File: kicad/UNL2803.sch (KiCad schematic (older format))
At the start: 19 parts, among them P15 CONN_01X08, P16 CONN_01X08, U4 ULN2803

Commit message: cambios menores
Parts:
- D10, D11, D12, D13, D6, D7, D8, D9: symbol LED -> LED-RESCUE-np08
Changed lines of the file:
@@
 EESchema Schematic File Version 2
+LIBS:np08-rescue
 LIBS:power
 LIBS:device
@@
 	7300 4500 6900 4500
 $Comp
-L LED D6
+L LED-RESCUE-np08 D6
 U 1 1 57A4DC0A
 P 7900 3800
+AR Path="/57A4DC0A" Ref="D6"  Part="1"
+AR Path="/57A4D8D4/57A4DC0A" Ref="D6"  Part="1"
 F 0 "D6" H 7900 3900 50  0000 C CNN
 F 1 "LED" H 7900 3700 50  0000 C CNN
@@
 $EndComp
 $Comp
-L LED D7
+L LED-RESCUE-np08 D7
 U 1 1 57A4DC4B
 P 8200 3900
+AR Path="/57A4DC4B" Ref="D7"  Part="1"
+AR Path="/57A4D8D4/57A4DC4B" Ref="D7"  Part="1"
 F 0 "D7" H 8200 4000 50  0000 C CNN
 F 1 "LED" H 8200 3800 50  0000 C CNN
@@
 $EndComp
 $Comp
-L LED D8
+L LED-RESCUE-np08 D8
 U 1 1 57A4DC8A
 P 8500 4000
+AR Path="/57A4DC8A" Ref="D8"  Part="1"
+AR Path="/57A4D8D4/57A4DC8A" Ref="D8"  Part="1"
 F 0 "D8" H 8500 4100 50  0000 C CNN
 F 1 "LED" H 8500 3900 50  0000 C CNN
@@
 $EndComp
 $Comp
-L LED D9
+L LED-RESCUE-np08 D9
 U 1 1 57A4DCFC
 P 8800 4100
+AR Path="/57A4DCFC" Ref="D9"  Part="1"
+AR Path="/57A4D8D4/57A4DCFC" Ref="D9"  Part="1"
 F 0 "D9" H 8800 4200 50  0000 C CNN
 F 1 "LED" H 8800 4000 50  0000 C CNN
@@
 $EndComp
 $Comp
-L LED D10
+L LED-RESCUE-np08 D10
 U 1 1 57A4DE04
 P 9100 4200
+AR Path="/57A4DE04" Ref="D10"  Part="1"
+AR Path="/57A4D8D4/57A4DE04" Ref="D10"  Part="1"
 F 0 "D10" H 9100 4300 50  0000 C CNN
 F 1 "LED" H 9100 4100 50  0000 C CNN
@@
 $EndComp
 $Comp
-L LED D11
+L LED-RESCUE-np08 D11
 U 1 1 57A4DE4E
 P 9400 4300
+AR Path="/57A4DE4E" Ref="D11"  Part="1"
+AR Path="/57A4D8D4/57A4DE4E" Ref="D11"  Part="1"
 F 0 "D11" H 9400 4400 50  0000 C CNN
 F 1 "LED" H 9400 4200 50  0000 C CNN
@@
 $EndComp
 $Comp
-L LED D12
+L LED-RESCUE-np08 D12
 U 1 1 57A4DEA5
 P 9700 4400
+AR Path="/57A4DEA5" Ref="D12"  Part="1"
+AR Path="/57A4D8D4/57A4DEA5" Ref="D12"  Part="1"
 F 0 "D12" H 9700 4500 50  0000 C CNN
 F 1 "LED" H 9700 4300 50  0000 C CNN
@@
 	9500 4400 7400 4400
 $Comp
-L LED D13
+L LED-RESCUE-np08 D13
 U 1 1 57A4E19D
 P 10000 4500
+AR Path="/57A4E19D" Ref="D13"  Part="1"
+AR Path="/57A4D8D4/57A4E19D" Ref="D13"  Part="1"
 F 0 "D13" H 10000 4600 50  0000 C CNN
 F 1 "LED" H 10000 4400 50  0000 C CNN

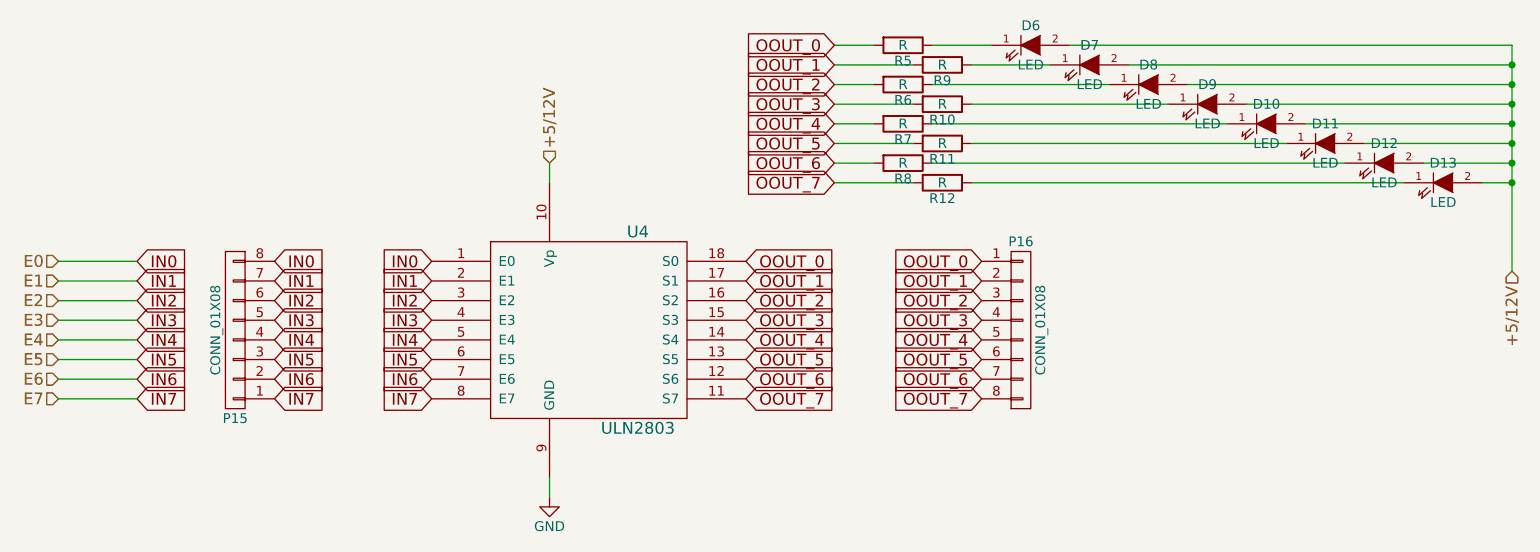
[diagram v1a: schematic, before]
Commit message: cambios en la placa np08
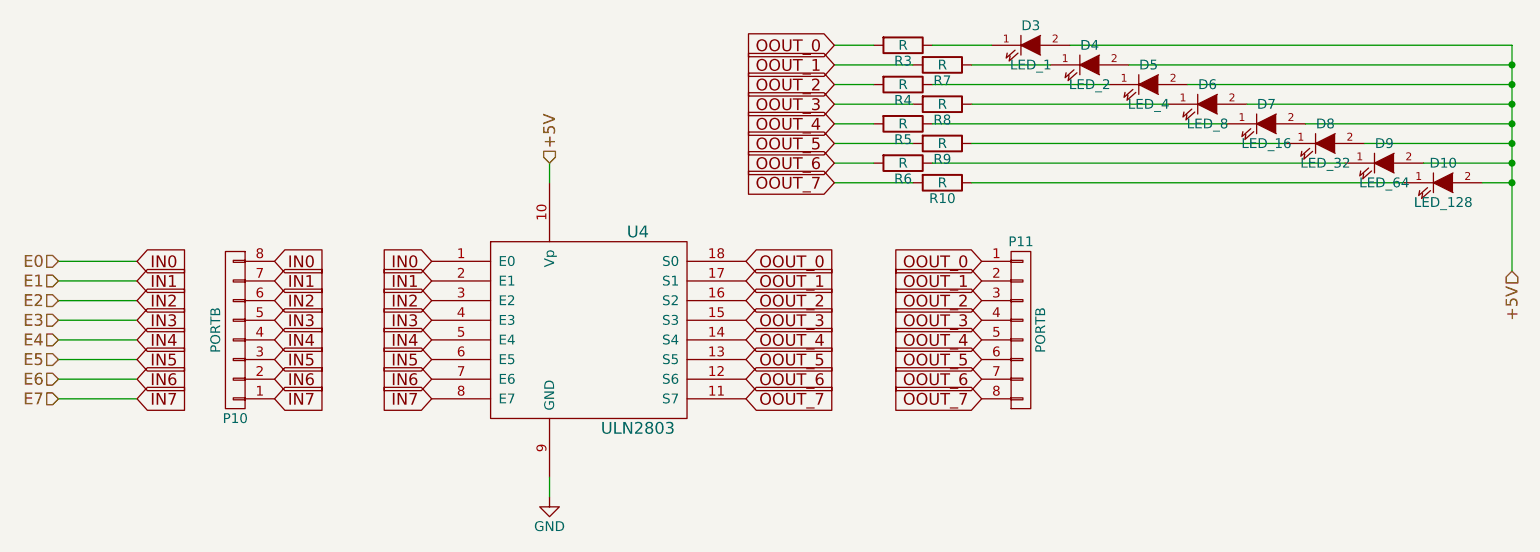
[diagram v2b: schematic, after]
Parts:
- D10: renamed from D13; value LED -> LED_128; footprint LEDs:LED-5MM -> LEDs:LED_D5.0mm
- D3: renamed from D6; value LED -> LED_1; footprint LEDs:LED-5MM -> LEDs:LED_D5.0mm
- D4: renamed from D7; value LED -> LED_2; footprint LEDs:LED-5MM -> LEDs:LED_D5.0mm
- D5: renamed from D8; value LED -> LED_4; footprint LEDs:LED-5MM -> LEDs:LED_D5.0mm
- D6: renamed from D9; value LED -> LED_8; footprint LEDs:LED-5MM -> LEDs:LED_D5.0mm
- D7: renamed from D10; value LED -> LED_16; footprint LEDs:LED-5MM -> LEDs:LED_D5.0mm
- D8: renamed from D11; value LED -> LED_32; footprint LEDs:LED-5MM -> LEDs:LED_D5.0mm
- D9: renamed from D12; value LED -> LED_64; footprint LEDs:LED-5MM -> LEDs:LED_D5.0mm
- P10: renamed from P15; value CONN_01X08 -> PORTB; footprint Pin_Headers:Pin_Header_Straight_1x08 -> Pin_Headers:Pin_Header_Straight_1x08_Pitch2.54mm
- P11: renamed from P16; value CONN_01X08 -> PORTB; footprint Pin_Headers:Pin_Header_Straight_1x08 -> Pin_Headers:Pin_Header_Straight_1x08_Pitch2.54mm
- R10: renamed from R12; footprint Resistors_ThroughHole:Resistor_Horizontal_RM7mm -> Resistors_THT:R_Axial_DIN0411_L9.9mm_D3.6mm_P12.70mm_Horizontal
- R3: renamed from R5; footprint Resistors_ThroughHole:Resistor_Horizontal_RM7mm -> Resistors_THT:R_Axial_DIN0411_L9.9mm_D3.6mm_P12.70mm_Horizontal
- R4: renamed from R6; footprint Resistors_ThroughHole:Resistor_Horizontal_RM7mm -> Resistors_THT:R_Axial_DIN0411_L9.9mm_D3.6mm_P12.70mm_Horizontal
- R5: renamed from R7; footprint Resistors_ThroughHole:Resistor_Horizontal_RM7mm -> Resistors_THT:R_Axial_DIN0411_L9.9mm_D3.6mm_P12.70mm_Horizontal
- R6: renamed from R8; footprint Resistors_ThroughHole:Resistor_Horizontal_RM7mm -> Resistors_THT:R_Axial_DIN0411_L9.9mm_D3.6mm_P12.70mm_Horizontal
- R7: renamed from R9; footprint Resistors_ThroughHole:Resistor_Horizontal_RM7mm -> Resistors_THT:R_Axial_DIN0411_L9.9mm_D3.6mm_P12.70mm_Horizontal
- R8: renamed from R10; footprint Resistors_ThroughHole:Resistor_Horizontal_RM7mm -> Resistors_THT:R_Axial_DIN0411_L9.9mm_D3.6mm_P12.70mm_Horizontal
- R9: renamed from R11; footprint Resistors_ThroughHole:Resistor_Horizontal_RM7mm -> Resistors_THT:R_Axial_DIN0411_L9.9mm_D3.6mm_P12.70mm_Horizontal
- U4: footprint Housings_DIP:DIP-18_W7.62mm -> Housings_DIP:DIP-18_W7.62mm_LongPads
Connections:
- net +5/12V renamed +5V
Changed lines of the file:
@@
 F 0 "U4" H 5900 5750 60  0000 C CNN
 F 1 "ULN2803" H 5900 4750 60  0000 C CNN
-F 2 "Housings_DIP:DIP-18_W7.62mm" H 5650 5250 60  0001 C CNN
+F 2 "Housings_DIP:DIP-18_W7.62mm_LongPads" H 5650 5250 60  0001 C CNN
 F 3 "" H 5650 5250 60  0000 C CNN
 	1    5650 5250
@@
 $EndComp
 $Comp
-L GND #PWR022
+L GND #PWR033
 U 1 1 57A4D9B4
 P 5450 6100
-F 0 "#PWR022" H 5450 5850 50  0001 C CNN
+F 0 "#PWR033" H 5450 5850 50  0001 C CNN
 F 1 "GND" H 5450 5950 50  0000 C CNN
 F 2 "" H 5450 6100 50  0000 C CNN
@@
 	5450 6100 5450 6000
 $Comp
-L R R5
+L R R3
 U 1 1 57A4D9CE
 P 7250 3800
-F 0 "R5" V 7330 3800 50  0000 C CNN
+F 0 "R3" V 7330 3800 50  0000 C CNN
 F 1 "R" V 7250 3800 50  0000 C CNN
-F 2 "Resistors_ThroughHole:Resistor_Horizontal_RM7mm" V 7180 3800 50  0001 C CNN
+F 2 "Resistors_THT:R_Axial_DIN0411_L9.9mm_D3.6mm_P12.70mm_Horizontal" V 7180 3800 50  0001 C CNN
 F 3 "" H 7250 3800 50  0000 C CNN
 	1    7250 3800
@@
 $EndComp
 $Comp
-L R R9
+L R R7
 U 1 1 57A4DA37
 P 7450 3900
-F 0 "R9" V 7530 3900 50  0000 C CNN
+F 0 "R7" V 7530 3900 50  0000 C CNN
 F 1 "R" V 7450 3900 50  0000 C CNN
-F 2 "Resistors_ThroughHole:Resistor_Horizontal_RM7mm" V 7380 3900 50  0001 C CNN
+F 2 "Resistors_THT:R_Axial_DIN0411_L9.9mm_D3.6mm_P12.70mm_Horizontal" V 7380 3900 50  0001 C CNN
 F 3 "" H 7450 3900 50  0000 C CNN
 	1    7450 3900
@@
 $EndComp
 $Comp
-L R R6
+L R R4
 U 1 1 57A4DA6C
 P 7250 4000
-F 0 "R6" V 7330 4000 50  0000 C CNN
+F 0 "R4" V 7330 4000 50  0000 C CNN
 F 1 "R" V 7250 4000 50  0000 C CNN
-F 2 "Resistors_ThroughHole:Resistor_Horizontal_RM7mm" V 7180 4000 50  0001 C CNN
+F 2 "Resistors_THT:R_Axial_DIN0411_L9.9mm_D3.6mm_P12.70mm_Horizontal" V 7180 4000 50  0001 C CNN
 F 3 "" H 7250 4000 50  0000 C CNN
 	1    7250 4000
@@
 $EndComp
 $Comp
-L R R10
+L R R8
 U 1 1 57A4DA94
 P 7450 4100
-F 0 "R10" V 7530 4100 50  0000 C CNN
+F 0 "R8" V 7530 4100 50  0000 C CNN
 F 1 "R" V 7450 4100 50  0000 C CNN
-F 2 "Resistors_ThroughHole:Resistor_Horizontal_RM7mm" V 7380 4100 50  0001 C CNN
+F 2 "Resistors_THT:R_Axial_DIN0411_L9.9mm_D3.6mm_P12.70mm_Horizontal" V 7380 4100 50  0001 C CNN
 F 3 "" H 7450 4100 50  0000 C CNN
 	1    7450 4100
@@
 $EndComp
 $Comp
-L R R7
+L R R5
 U 1 1 57A4DABB
 P 7250 4200
-F 0 "R7" V 7330 4200 50  0000 C CNN
+F 0 "R5" V 7330 4200 50  0000 C CNN
 F 1 "R" V 7250 4200 50  0000 C CNN
-F 2 "Resistors_ThroughHole:Resistor_Horizontal_RM7mm" V 7180 4200 50  0001 C CNN
+F 2 "Resistors_THT:R_Axial_DIN0411_L9.9mm_D3.6mm_P12.70mm_Horizontal" V 7180 4200 50  0001 C CNN
 F 3 "" H 7250 4200 50  0000 C CNN
 	1    7250 4200
@@
 $EndComp
 $Comp
-L R R11
+L R R9
 U 1 1 57A4DAED
 P 7450 4300
-F 0 "R11" V 7530 4300 50  0000 C CNN
+F 0 "R9" V 7530 4300 50  0000 C CNN
 F 1 "R" V 7450 4300 50  0000 C CNN
-F 2 "Resistors_ThroughHole:Resistor_Horizontal_RM7mm" V 7380 4300 50  0001 C CNN
+F 2 "Resistors_THT:R_Axial_DIN0411_L9.9mm_D3.6mm_P12.70mm_Horizontal" V 7380 4300 50  0001 C CNN
 F 3 "" H 7450 4300 50  0000 C CNN
 	1    7450 4300
@@
 $EndComp
 $Comp
-L R R8
+L R R6
 U 1 1 57A4DB1E
 P 7250 4400
-F 0 "R8" V 7330 4400 50  0000 C CNN
+F 0 "R6" V 7330 4400 50  0000 C CNN
 F 1 "R" V 7250 4400 50  0000 C CNN
-F 2 "Resistors_ThroughHole:Resistor_Horizontal_RM7mm" V 7180 4400 50  0001 C CNN
+F 2 "Resistors_THT:R_Axial_DIN0411_L9.9mm_D3.6mm_P12.70mm_Horizontal" V 7180 4400 50  0001 C CNN
 F 3 "" H 7250 4400 50  0000 C CNN
 	1    7250 4400
@@
 $EndComp
 $Comp
-L R R12
+L R R10
 U 1 1 57A4DB5A
 P 7450 4500
-F 0 "R12" V 7530 4500 50  0000 C CNN
+F 0 "R10" V 7530 4500 50  0000 C CNN
 F 1 "R" V 7450 4500 50  0000 C CNN
-F 2 "Resistors_ThroughHole:Resistor_Horizontal_RM7mm" V 7380 4500 50  0001 C CNN
+F 2 "Resistors_THT:R_Axial_DIN0411_L9.9mm_D3.6mm_P12.70mm_Horizontal" V 7380 4500 50  0001 C CNN
 F 3 "" H 7450 4500 50  0000 C CNN
 	1    7450 4500
@@
 	7300 4500 6900 4500
 $Comp
-L LED-RESCUE-np08 D6
+L LED-RESCUE-np08 D3
 U 1 1 57A4DC0A
 P 7900 3800
-AR Path="/57A4DC0A" Ref="D6"  Part="1"
-AR Path="/57A4D8D4/57A4DC0A" Ref="D6"  Part="1"
-F 0 "D6" H 7900 3900 50  0000 C CNN
-F 1 "LED" H 7900 3700 50  0000 C CNN
-F 2 "LEDs:LED-5MM" H 7900 3800 50  0001 C CNN
+F 0 "D3" H 7900 3900 50  0000 C CNN
+F 1 "LED_1" H 7900 3700 50  0000 C CNN
+F 2 "LEDs:LED_D5.0mm" H 7900 3800 50  0001 C CNN
 F 3 "" H 7900 3800 50  0000 C CNN
 	1    7900 3800
@@
 $EndComp
 $Comp
-L LED-RESCUE-np08 D7
+L LED-RESCUE-np08 D4
 U 1 1 57A4DC4B
 P 8200 3900
-AR Path="/57A4DC4B" Ref="D7"  Part="1"
-AR Path="/57A4D8D4/57A4DC4B" Ref="D7"  Part="1"
-F 0 "D7" H 8200 4000 50  0000 C CNN
-F 1 "LED" H 8200 3800 50  0000 C CNN
-F 2 "LEDs:LED-5MM" H 8200 3900 50  0001 C CNN
+F 0 "D4" H 8200 4000 50  0000 C CNN
+F 1 "LED_2" H 8200 3800 50  0000 C CNN
+F 2 "LEDs:LED_D5.0mm" H 8200 3900 50  0001 C CNN
 F 3 "" H 8200 3900 50  0000 C CNN
 	1    8200 3900
@@
 $EndComp
 $Comp
-L LED-RESCUE-np08 D8
+L LED-RESCUE-np08 D5
 U 1 1 57A4DC8A
 P 8500 4000
-AR Path="/57A4DC8A" Ref="D8"  Part="1"
-AR Path="/57A4D8D4/57A4DC8A" Ref="D8"  Part="1"
-F 0 "D8" H 8500 4100 50  0000 C CNN
-F 1 "LED" H 8500 3900 50  0000 C CNN
-F 2 "LEDs:LED-5MM" H 8500 4000 50  0001 C CNN
+F 0 "D5" H 8500 4100 50  0000 C CNN
+F 1 "LED_4" H 8500 3900 50  0000 C CNN
+F 2 "LEDs:LED_D5.0mm" H 8500 4000 50  0001 C CNN
 F 3 "" H 8500 4000 50  0000 C CNN
 	1    8500 4000
@@
 $EndComp
 $Comp
-L LED-RESCUE-np08 D9
+L LED-RESCUE-np08 D6
 U 1 1 57A4DCFC
 P 8800 4100
-AR Path="/57A4DCFC" Ref="D9"  Part="1"
-AR Path="/57A4D8D4/57A4DCFC" Ref="D9"  Part="1"
-F 0 "D9" H 8800 4200 50  0000 C CNN
-F 1 "LED" H 8800 4000 50  0000 C CNN
-F 2 "LEDs:LED-5MM" H 8800 4100 50  0001 C CNN
+F 0 "D6" H 8800 4200 50  0000 C CNN
+F 1 "LED_8" H 8800 4000 50  0000 C CNN
+F 2 "LEDs:LED_D5.0mm" H 8800 4100 50  0001 C CNN
 F 3 "" H 8800 4100 50  0000 C CNN
 	1    8800 4100
@@
 $EndComp
 $Comp
-L LED-RESCUE-np08 D10
+L LED-RESCUE-np08 D7
 U 1 1 57A4DE04
 P 9100 4200
-AR Path="/57A4DE04" Ref="D10"  Part="1"
-AR Path="/57A4D8D4/57A4DE04" Ref="D10"  Part="1"
-F 0 "D10" H 9100 4300 50  0000 C CNN
-F 1 "LED" H 9100 4100 50  0000 C CNN
-F 2 "LEDs:LED-5MM" H 9100 4200 50  0001 C CNN
+F 0 "D7" H 9100 4300 50  0000 C CNN
+F 1 "LED_16" H 9100 4100 50  0000 C CNN
+F 2 "LEDs:LED_D5.0mm" H 9100 4200 50  0001 C CNN
 F 3 "" H 9100 4200 50  0000 C CNN
 	1    9100 4200
@@
 $EndComp
 $Comp
-L LED-RESCUE-np08 D11
+L LED-RESCUE-np08 D8
 U 1 1 57A4DE4E
 P 9400 4300
-AR Path="/57A4DE4E" Ref="D11"  Part="1"
-AR Path="/57A4D8D4/57A4DE4E" Ref="D11"  Part="1"
-F 0 "D11" H 9400 4400 50  0000 C CNN
-F 1 "LED" H 9400 4200 50  0000 C CNN
-F 2 "LEDs:LED-5MM" H 9400 4300 50  0001 C CNN
+F 0 "D8" H 9400 4400 50  0000 C CNN
+F 1 "LED_32" H 9400 4200 50  0000 C CNN
+F 2 "LEDs:LED_D5.0mm" H 9400 4300 50  0001 C CNN
 F 3 "" H 9400 4300 50  0000 C CNN
 	1    9400 4300
@@
 $EndComp
 $Comp
-L LED-RESCUE-np08 D12
+L LED-RESCUE-np08 D9
 U 1 1 57A4DEA5
 P 9700 4400
-AR Path="/57A4DEA5" Ref="D12"  Part="1"
-AR Path="/57A4D8D4/57A4DEA5" Ref="D12"  Part="1"
-F 0 "D12" H 9700 4500 50  0000 C CNN
-F 1 "LED" H 9700 4300 50  0000 C CNN
-F 2 "LEDs:LED-5MM" H 9700 4400 50  0001 C CNN
+F 0 "D9" H 9700 4500 50  0000 C CNN
+F 1 "LED_64" H 9700 4300 50  0000 C CNN
+F 2 "LEDs:LED_D5.0mm" H 9700 4400 50  0001 C CNN
 F 3 "" H 9700 4400 50  0000 C CNN
 	1    9700 4400
@@
 	9500 4400 7400 4400
 $Comp
-L LED-RESCUE-np08 D13
+L LED-RESCUE-np08 D10
 U 1 1 57A4E19D
 P 10000 4500
-AR Path="/57A4E19D" Ref="D13"  Part="1"
-AR Path="/57A4D8D4/57A4E19D" Ref="D13"  Part="1"
-F 0 "D13" H 10000 4600 50  0000 C CNN
-F 1 "LED" H 10000 4400 50  0000 C CNN
-F 2 "LEDs:LED-5MM" H 10000 4500 50  0001 C CNN
+F 0 "D10" H 10000 4600 50  0000 C CNN
+F 1 "LED_128" H 10000 4400 50  0000 C CNN
+F 2 "LEDs:LED_D5.0mm" H 10000 4500 50  0001 C CNN
 F 3 "" H 10000 4500 50  0000 C CNN
 	1    10000 4500
@@
 Connection ~ 10350 3900
 Text HLabel 10350 4950 3    60   Input ~ 0
-+5/12V
++5V
 Text HLabel 5450 4400 1    60   Input ~ 0
-+5/12V
++5V
 Wire Wire Line
 	5450 4500 5450 4400
@@
 OOUT_7
 $Comp
-L CONN_01X08 P16
+L CONN_01X08 P11
 U 1 1 57A50263
 P 7850 5250
-F 0 "P16" H 7850 5700 50  0000 C CNN
-F 1 "CONN_01X08" V 7950 5250 50  0000 C CNN
-F 2 "Pin_Headers:Pin_Header_Straight_1x08" H 7850 5250 50  0001 C CNN
+F 0 "P11" H 7850 5700 50  0000 C CNN
+F 1 "PORTB" V 7950 5250 50  0000 C CNN
+F 2 "Pin_Headers:Pin_Header_Straight_1x08_Pitch2.54mm" H 7850 5250 50  0001 C CNN
 F 3 "" H 7850 5250 50  0000 C CNN
 	1    7850 5250
@@
 IN7
 $Comp
-L CONN_01X08 P15
+L CONN_01X08 P10
 U 1 1 57A50832
 P 3850 5250
-F 0 "P15" H 3850 5700 50  0000 C CNN
-F 1 "CONN_01X08" V 3950 5250 50  0000 C CNN
-F 2 "Pin_Headers:Pin_Header_Straight_1x08" H 3850 5250 50  0001 C CNN
+F 0 "P10" H 3850 5700 50  0000 C CNN
+F 1 "PORTB" V 3950 5250 50  0000 C CNN
+F 2 "Pin_Headers:Pin_Header_Straight_1x08_Pitch2.54mm" H 3850 5250 50  0001 C CNN
 F 3 "" H 3850 5250 50  0000 C CNN
 	1    3850 5250

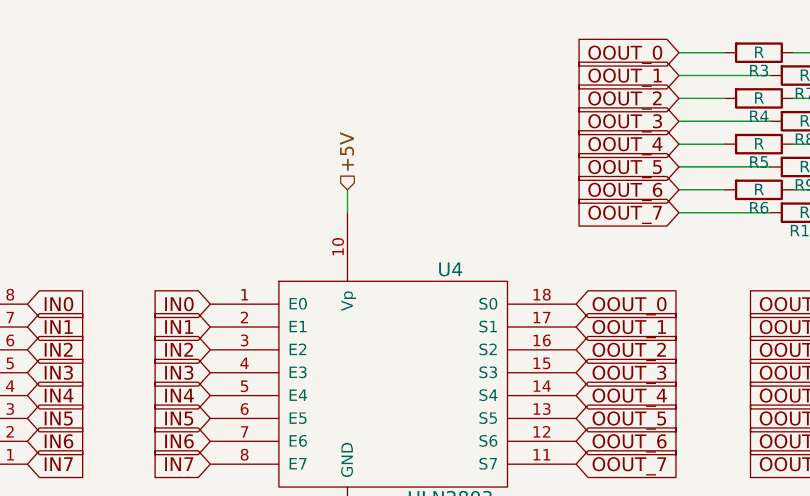
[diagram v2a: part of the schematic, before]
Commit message: arreglando la fuente de alimentación, los servos estaban conectados al 78l05
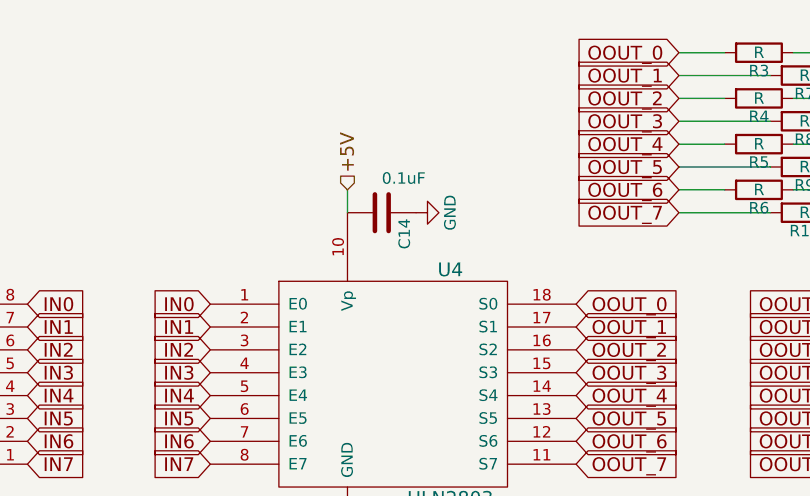
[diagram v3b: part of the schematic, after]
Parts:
- added C14: 0.1uF, Capacitors_THT:C_Disc_D3.4mm_W2.1mm_P2.50mm, symbol C
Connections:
- net +5V: now also C14.2
- net GND: now also C14.1
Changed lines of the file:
@@
 $EndComp
 $Comp
-L GND #PWR033
+L GND #PWR027
 U 1 1 57A4D9B4
 P 5450 6100
-F 0 "#PWR033" H 5450 5850 50  0001 C CNN
+F 0 "#PWR027" H 5450 5850 50  0001 C CNN
 F 1 "GND" H 5450 5950 50  0000 C CNN
 F 2 "" H 5450 6100 50  0000 C CNN
@@
 Text GLabel 4850 5600 0    60   Input ~ 0
 IN7
+$Comp
+L C C14
+U 1 1 59C1B73B
+P 5600 4500
+F 0 "C14" H 5625 4600 50  0000 L CNN
+F 1 "0.1uF" V 5450 4500 50  0000 L CNN
+F 2 "Capacitors_THT:C_Disc_D3.4mm_W2.1mm_P2.50mm" H 5638 4350 50  0001 C CNN
+F 3 "" H 5600 4500 50  0001 C CNN
+	1    5600 4500
+	0    1    1    0
+$EndComp
+$Comp
+L GND #PWR028
+U 1 1 59C1B81C
+P 5750 4500
+F 0 "#PWR028" H 5750 4250 50  0001 C CNN
+F 1 "GND" H 5750 4350 50  0000 C CNN
+F 2 "" H 5750 4500 50  0000 C CNN
+F 3 "" H 5750 4500 50  0000 C CNN
+	1    5750 4500
+	0    -1   -1   0
+$EndComp
 $EndSCHEMATC
